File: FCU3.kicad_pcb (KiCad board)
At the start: 4 copper layers, 36.7 x 36.7 mm, 54 parts, among them J1 SM06B-SRSS-TB_LF__SN_, J2 SM06B-SRSS-TB_LF__SN_, J4 SM08B-SRSS-TB_LF__SN_, J6 UJ20-C-H-G-SMT-1-P16-TR, Q2 SS8050, U1 MPU-6500, U3 MCP1700x-330xxTT, U5 STM32F405RGTx, Y1 LFXTAL055207Bulk

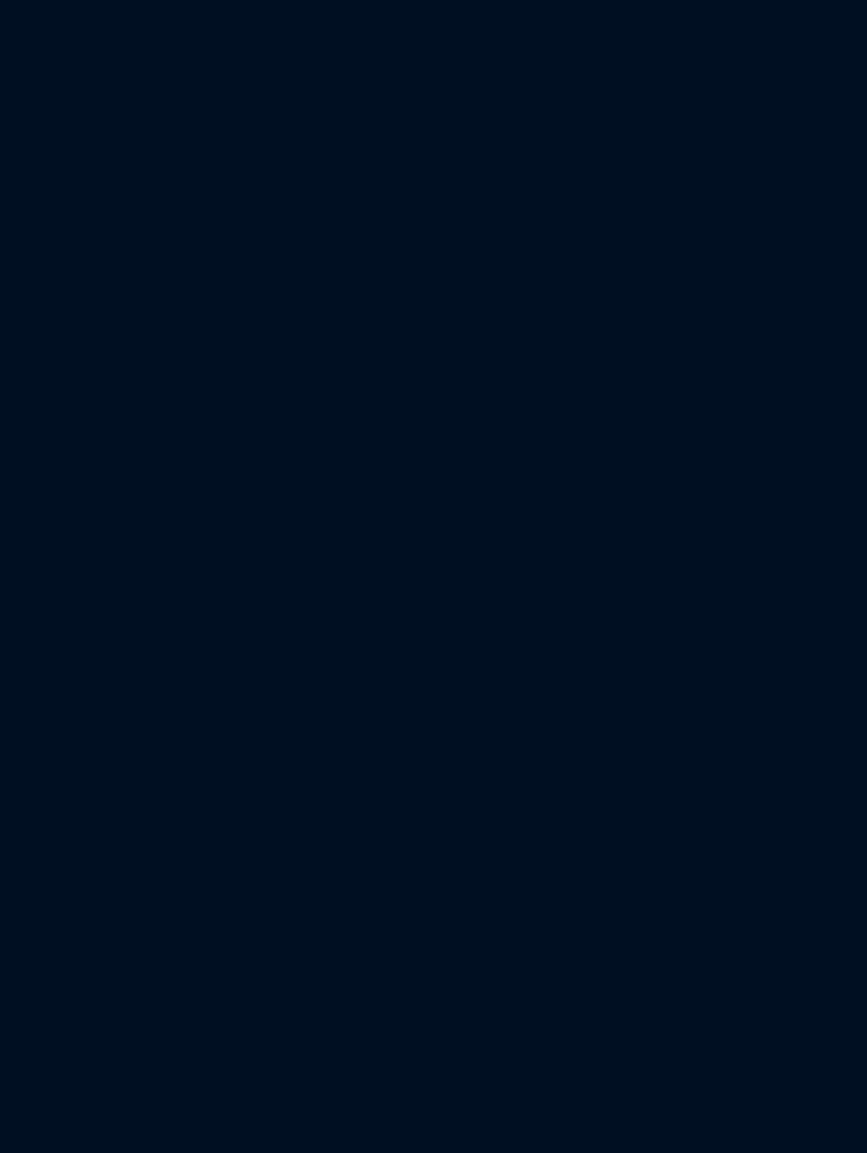
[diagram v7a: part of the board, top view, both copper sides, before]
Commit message: Added part-numbers and updated symbols
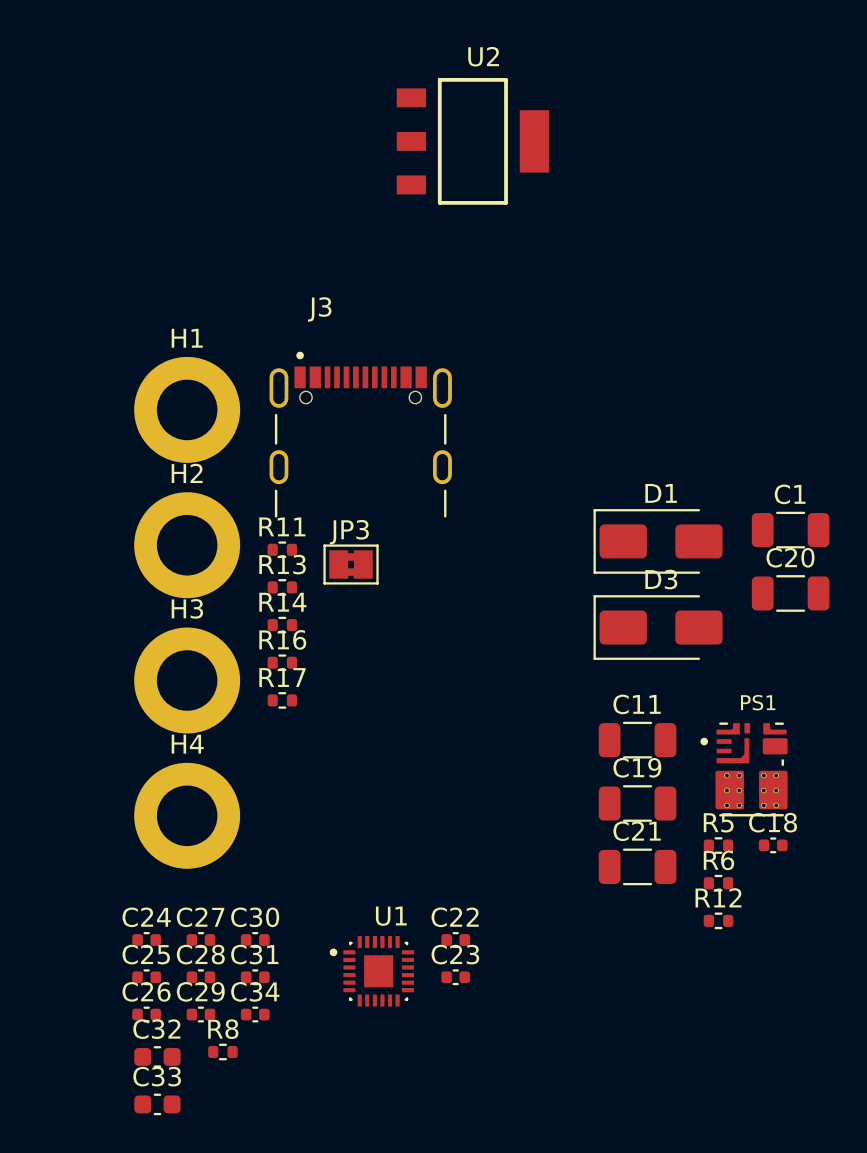
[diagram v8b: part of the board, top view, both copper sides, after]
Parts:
- added C1: 1uF, Capacitor_SMD:C_1206_3216Metric, F.Cu at (220.5, 81.2)
- added C11: 22uF, Capacitor_SMD:C_1206_3216Metric, F.Cu at (212.4, 92.3)
- added C18: 100nF, Capacitor_SMD:C_0402_1005Metric, F.Cu at (219.6, 97.9)
- added C19: 22uF, Capacitor_SMD:C_1206_3216Metric, F.Cu at (212.4, 95.7)
- added C20: 1uF, Capacitor_SMD:C_1206_3216Metric, F.Cu at (220.5, 84.6)
- added C21: 22uF, Capacitor_SMD:C_1206_3216Metric, F.Cu at (212.4, 99.0)
- added C22: 100nF, Capacitor_SMD:C_0402_1005Metric, F.Cu at (202.8, 102.9)
- added C23: 100nF, Capacitor_SMD:C_0402_1005Metric, F.Cu at (202.8, 104.9)
- added C24: 100nF, Capacitor_SMD:C_0402_1005Metric, F.Cu at (186.5, 102.9)
- added C25: 100nF, Capacitor_SMD:C_0402_1005Metric, F.Cu at (186.5, 104.9)
- added C26: 100nF, Capacitor_SMD:C_0402_1005Metric, F.Cu at (186.5, 106.8)
- added C27: 100nF, Capacitor_SMD:C_0402_1005Metric, F.Cu at (189.4, 102.9)
- added C28: 100nF, Capacitor_SMD:C_0402_1005Metric, F.Cu at (189.4, 104.9)
- added C29: 2.2uF, Capacitor_SMD:C_0402_1005Metric, F.Cu at (189.4, 106.8)
- added C30: 2.2uF, Capacitor_SMD:C_0402_1005Metric, F.Cu at (192.2, 102.9)
- added C31: 2.2uF, Capacitor_SMD:C_0402_1005Metric, F.Cu at (192.2, 104.9)
- added C32: 27pF, Capacitor_SMD:C_0603_1608Metric, F.Cu at (187.1, 109.1)
- added C33: 27pF, Capacitor_SMD:C_0603_1608Metric, F.Cu at (187.1, 111.6)
- added C34: 10uF, Capacitor_SMD:C_0402_1005Metric, F.Cu at (192.2, 106.8)
- added D1: SS14-M3/5AT, Diode_SMD:D_SMA, F.Cu at (213.7, 81.8)
- added D3: SS14-M3/5AT, Diode_SMD:D_SMA, F.Cu at (213.7, 86.4)
- added H1: MountingHole_Pad_MP, MountingHole:MountingHole_3.2mm_M3_DIN965_Pad, F.Cu at (188.7, 74.9)
- added H2: MountingHole_Pad_MP, MountingHole:MountingHole_3.2mm_M3_DIN965_Pad, F.Cu at (188.7, 82.0)
- added H3: MountingHole_Pad_MP, MountingHole:MountingHole_3.2mm_M3_DIN965_Pad, F.Cu at (188.7, 89.2)
- added H4: MountingHole_Pad_MP, MountingHole:MountingHole_3.2mm_M3_DIN965_Pad, F.Cu at (188.7, 96.3)
- added J3: UJ20-C-H-G-SMT-1-P16-TR, KSE_connector:SAMESKY_UJ20-C-H-G-SMT-1-P16-TR, F.Cu at (197.8, 80.5)
- added JP3: SolderJumper_2_Bridged, Jumper:SolderJumper-2_P1.3mm_Bridged2Bar_Pad1.0x1.5mm, F.Cu at (197.3, 83.1)
- added PS1: TPSM84338RCJR, KSE_DCDC:TPSM84338RCJR, F.Cu at (218.5, 93.9)
- added R11: 10k, Resistor_SMD:R_0402_1005Metric, F.Cu at (193.7, 82.3)
- added R12: 18k, Resistor_SMD:R_0402_1005Metric, F.Cu at (216.7, 101.9)
- added R13: 10k, Resistor_SMD:R_0402_1005Metric, F.Cu at (193.7, 84.3)
- added R14: 75k, Resistor_SMD:R_0402_1005Metric, F.Cu at (193.7, 86.3)
- added R16: 5.1k, Resistor_SMD:R_0402_1005Metric, F.Cu at (193.7, 88.2)
- added R17: 5.1k, Resistor_SMD:R_0402_1005Metric, F.Cu at (193.7, 90.2)
- added R5: 10k, Resistor_SMD:R_0402_1005Metric, F.Cu at (216.7, 97.9)
- added R6: 140k, Resistor_SMD:R_0402_1005Metric, F.Cu at (216.7, 99.9)
- added R8: 10k, Resistor_SMD:R_0402_1005Metric, F.Cu at (190.5, 108.8)
- added U1: MPU-6500, KSE_sensor:QFN40P300X300X95-25N, F.Cu at (198.8, 104.6)
- added U2: NCV4274AST33T3G, KSE_DCDC:SOT230P700X175-4N, F.Cu at (203.8, 60.7)
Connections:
- net /(lib_symbols/I2C1_SCL renamed /Project Architecture/I2C1_SCL
- net /(lib_symbols/I2C1_SDA renamed /Project Architecture/I2C1_SDA
- net /(lib_symbols/Microcontroller/LED0 renamed /Project Architecture/Microcontroller/LED0
- net /(lib_symbols/Microcontroller/LED1 renamed /Project Architecture/Microcontroller/LED1
- net /(lib_symbols/SBUS_TX renamed /Project Architecture/SBUS_TX
- net /(lib_symbols/UART4_RX renamed /Project Architecture/UART4_RX
- net /(lib_symbols/UART4_TX renamed /Project Architecture/UART4_TX
- net /(lib_symbols/UART5_RX renamed /Project Architecture/UART5_RX
- net /(lib_symbols/UART5_TX renamed /Project Architecture/UART5_TX
- Q2 pad 3: /(lib_symbols/UART2_RX -> /Project Architecture/UART2_RX
- S1 pad 1: /(lib_symbols/Microcontroller/DFU_Enable -> /Project Architecture/Microcontroller/DFU_Enable
- U5 pad 17: /(lib_symbols/UART2_RX -> /Project Architecture/UART2_RX
- U5 pad 20: /(lib_symbols/DIG_IMU_CS -> /Project Architecture/DIG_IMU_CS
- U5 pad 21: /(lib_symbols/SPI1_SCK -> /Project Architecture/SPI1_SCK
- U5 pad 22: /(lib_symbols/SPI1_SDI -> /Project Architecture/SPI1_SDI
- U5 pad 23: /(lib_symbols/SPI1_SDO -> /Project Architecture/SPI1_SDO
- U5 pad 24: /(lib_symbols/DIG_IMU_EXTI -> /Project Architecture/DIG_IMU_EXTI
- U5 pad 36: /(lib_symbols/ESC_SIG_M3 -> /Project Architecture/ESC_SIG_M3
- U5 pad 39: /(lib_symbols/ESC_SIG_M4 -> /Project Architecture/ESC_SIG_M4
- U5 pad 40: /(lib_symbols/ESC_SIG_M2 -> /Project Architecture/ESC_SIG_M2
- U5 pad 41: /(lib_symbols/ESC_SIG_M1 -> /Project Architecture/ESC_SIG_M1
- U5 pad 43: /(lib_symbols/UART1_RX -> /Project Architecture/UART1_RX
- U5 pad 44: /(lib_symbols/USB_+DATA -> /Project Architecture/USB_+DATA
- U5 pad 45: /(lib_symbols/USB_-DATA -> /Project Architecture/USB_-DATA
- U5 pad 5: /(lib_symbols/Microcontroller/CLK_OUT -> /Project Architecture/Microcontroller/CLK_OUT
- U5 pad 60: /(lib_symbols/Microcontroller/DFU_Enable -> /Project Architecture/Microcontroller/DFU_Enable
- U5 pad 8: /(lib_symbols/ANA_ADC_VBAT -> /Project Architecture/ANA_ADC_VBAT
- U5 pad 9: /(lib_symbols/ANA_ADC_CURR -> /Project Architecture/ANA_ADC_CURR
- Y1 pad 1: /(lib_symbols/Microcontroller/CLK_OUT -> /Project Architecture/Microcontroller/CLK_OUT
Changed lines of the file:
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@@
 	(property "DESIGNER" "Kaldstrand")
 	(property "FABRICATION_NOTES" "FABRICATION NOTES (UNLESS OTHERWISE SPECIFIED)\n\n1)	FABRICATE PER IPC-6012A CLASS 2.\n\n2)	OUTLINE DEFINED IN SEPARATE GERBER FILE WITH\n	\"Edge_Cuts.GBR\" SUFFIX.\n\n	DIMENSIONS OF CIRCUMSIZED RECTANGLE SHOWN ON THIS\n	DRAWING FOR REFERENCE ONLY.\n\n3)	SEE SEPARATE DRILL FILES WITH \".DRL\" SUFFIX \n	FOR HOLE LOCATIONS.\n\n	SELECTED HOLE LOCATIONS SHOWN ON THIS DRAWING \n	FOR REFERENCE ONLY.\n\n4)	SURFACE FINISH: IMMERSION GOLD\n\n5)	SOLDERMASK ON BOTH SIDES OF THE BOARD SHALL \n	BE LPI, COLOR BLACK.\n\n6)	SILK SCREEN LEGEND TO BE APPLIED PER LAYER \n	STACKUP USING YELLOW NON-CONDUCTIVE EPOXY INK.\n\n7)	ALL VIAS ARE TENTED ON BOTH SIDES UNLESS \n	SOLDERMASK OPENED IN GERBER.\n\n8)	VENDOR SHOULD FOLLOW ROHS COMPLIANT PROCESS \n	AND Pb FREE FOR MANUFACTURING\n\n9)	PCB MATERIAL REQUIREMENTS:\n\n	A.	FLAMMABILITY RATING MUST MEET OR EXCEED \n		UL94V-0 REQUIREMENTS.\n	B.	Tg 170 C OR EQUIVALENT.\n	C.	EQUIVALENT MATERIAL SHALL BE RoHS COMPLIANT, \n		HALOGEN FREE AND APPROVED BY KALDSTRAND ELECTRONICS.\n\n10)	DESIGN GEOMETRY MINIMUM FEATURE SIZES:\n\n	BOARD SIZE				36.700 × 36.700 mm\n	BOARD THICKNESS		1.660 mm\n	TRACE WIDTH			0.200 mm\n	TRACE TO TRACE		0.200 mm\n	MIN. HOLE (PTH)			0.200 mm\n	MIN. HOLE (NPTH)		0.650 mm\n	ANNULAR RING			0.050 mm\n	COPPER TO HOLE		0.254 mm\n	COPPER TO EDGE		0.250 mm\n	HOLE TO HOLE			0.254 mm\n\n11)	REFER TO IMPEDANCE TABLE FOR IMPEDANCE CONTROL REQUIREMENTS.\n\n12)	CONFIRM SPACE WIDTHS AND SPACINGS.")
-	(property "GIT_HASH_PCB" "5b377db")
-	(property "GIT_HASH_SCH" "5b377db")
+	(property "GIT_HASH_PCB" "4dadb50")
+	(property "GIT_HASH_SCH" "4dadb50")
 	(property "GIT_URL" "https://github.com/nguyen-v/KDT_Hierarchical_KiBot")
 	(property "PROJECT_NAME" "Flight Controller 3")
@@
 	(property "RELEASE_BODY_1.1.0" "")
 	(property "RELEASE_BODY_UNRELEASED" "Version Unreleased not found.")
-	(property "RELEASE_DATE" "27-Nov-2025")
-	(property "RELEASE_DATE_NUM" "2025-11-27")
+	(property "RELEASE_DATE" "02-Dec-2025")
+	(property "RELEASE_DATE_NUM" "2025-12-02")
 	(property "RELEASE_TITLE_1.0.0" "")
 	(property "RELEASE_TITLE_1.0.1" "")
@@
 	(property "SHEET_NAME_5" "Inertial Measurement Unit")
 	(property "SHEET_NAME_6" "Power")
-	(property "SHEET_NAME_7" "Revision History")
-	(property "SHEET_NAME_8" "......................................")
+	(property "SHEET_NAME_7" "10–26V to 9V2A Step-Down Converter")
+	(property "SHEET_NAME_8" "Revision History")
 	(property "SHEET_NAME_9" "......................................")
 	(property "VARIANT" "PRELIMINARY")
